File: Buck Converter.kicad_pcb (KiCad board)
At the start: 2 copper layers, 50 x 30 mm, 29 parts, among them J1 Conn_01x02, J2 Conn_01x02, SW1 SW_SPST, U1 LT3684xMSE

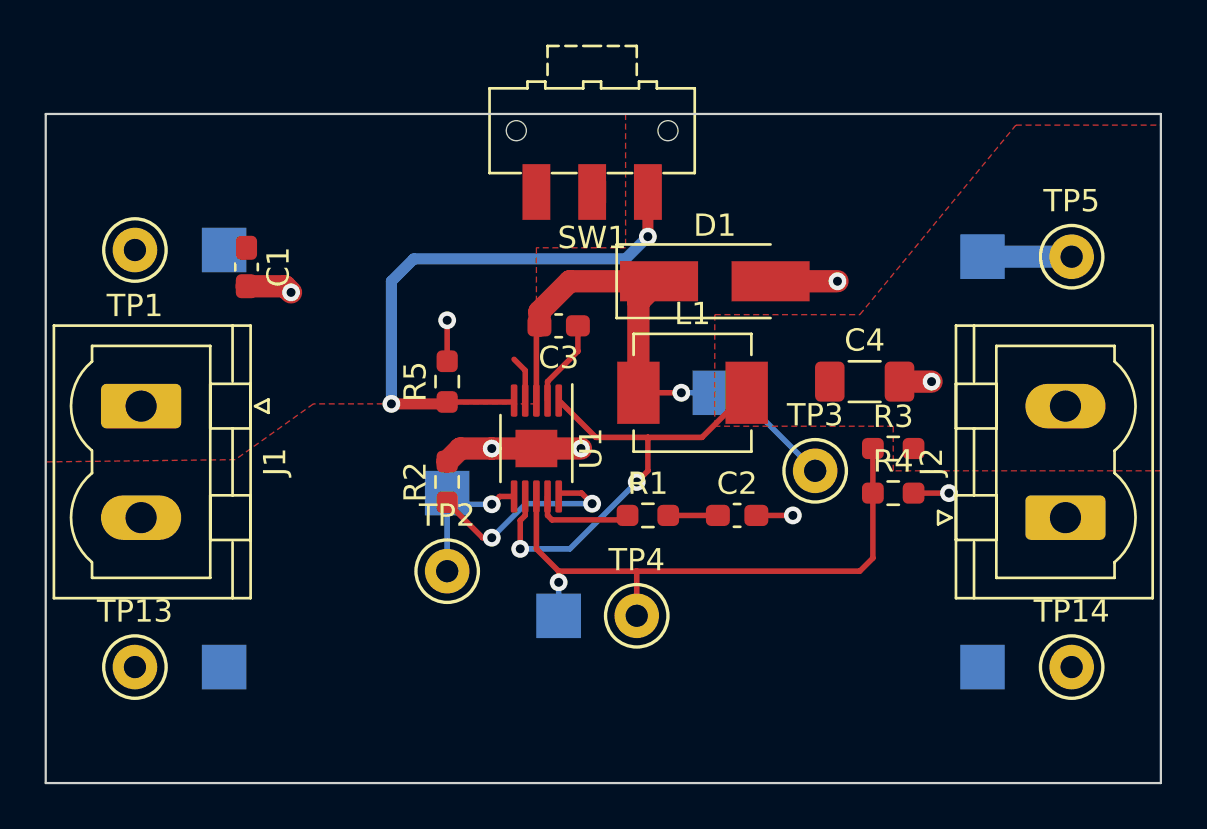
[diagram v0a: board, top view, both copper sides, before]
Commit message: Minor Tweaks
Updated PCB with the following recommendations:

1. Clean up the ERC and DRC issues.  The schematic has the USB connector without it being on the PCB; there's an unmade connection on TP6, and the silkscreen needs to be cleaned up.
2. Move the switch inward from the edge of the board.  The holes are close enough to the edge to cause some grief.
3. Move R5 a bit south.  It's an easy fix to clear up the path for VCC to get from J1.1 to U1.4.  Also to make way for:
3. Move C1 closer to the IC.  The bypass caps should be as close as possible to their associated ICs.
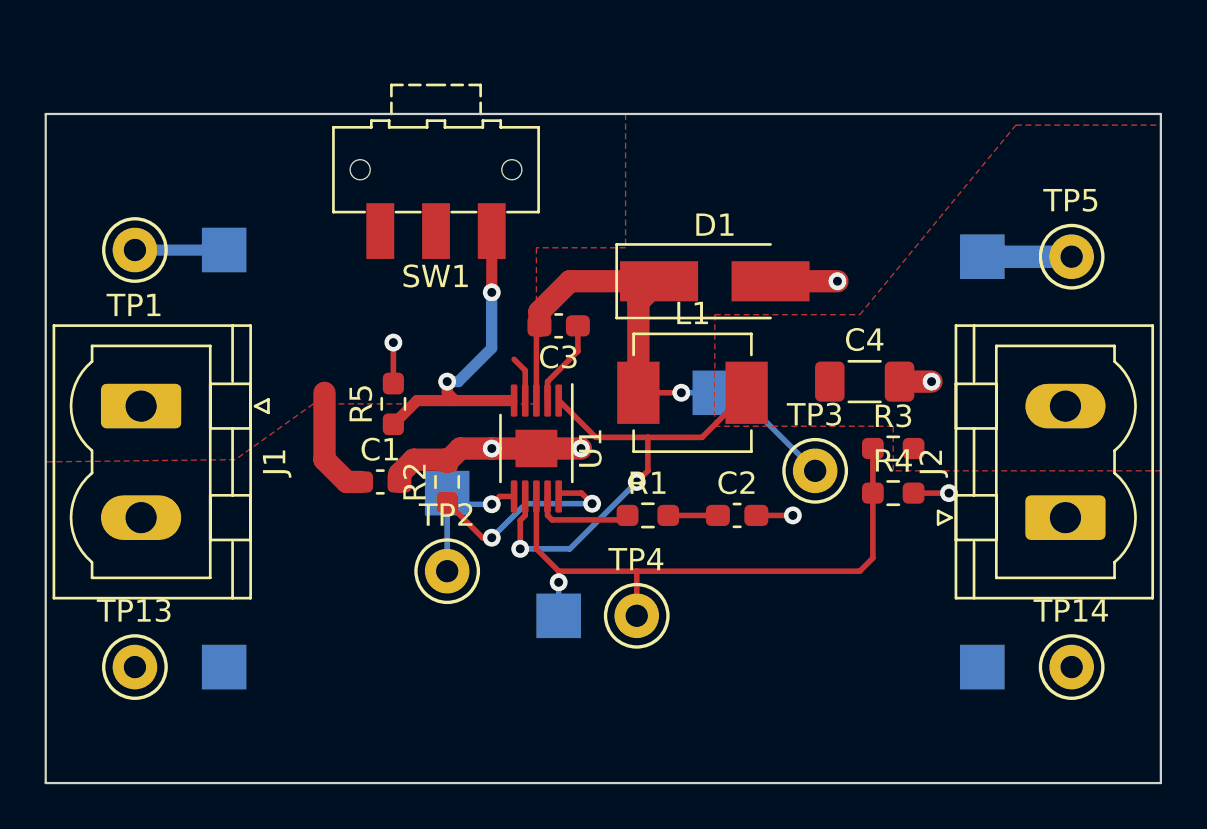
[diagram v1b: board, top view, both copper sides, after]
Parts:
- moved C1 11.4 mm to (115.0, 115.5), turned to 0 degrees
- moved SW1 7.22 mm to (117.5, 101.5)
- moved R5 2.61 mm to (115.6, 112.0)
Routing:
- net Net-(R5-Pad1): track 25.4 -> 15.1 mm
- net VCC: track 3.68 -> 11.3 mm
- net GND: track 17.9 -> 18.5 mm, vias 8 -> 7
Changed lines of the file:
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@@
   )
   (footprint "Resistor_SMD:R_0603_1608Metric_Pad0.98x0.95mm_HandSolder" (layer "F.Cu")
-    (at 118 111 90)
+    (at 115.5875 112 90)
     (descr "Resistor SMD 0603 (1608 Metric), square (rectangular) end terminal, IPC_7351 nominal with elongated pad for handsoldering. (Body size source: IPC-SM-782 page 72, https://www.pcb-3d.com/wordpress/wp-content/uploads/ipc-sm-782a_amendment_1_and_2.pdf), generated with kicad-footprint-generator")
     (tags "resistor handsolder")
@@
   )
   (footprint "Capacitor_SMD:C_0603_1608Metric_Pad1.08x0.95mm_HandSolder" (layer "F.Cu")
-    (at 109 105.8625 -90)
+    (at 115 115.5)
     (descr "Capacitor SMD 0603 (1608 Metric), square (rectangular) end terminal, IPC_7351 nominal with elongated pad for handsoldering. (Body size source: IPC-SM-782 page 76, https://www.pcb-3d.com/wordpress/wp-content/uploads/ipc-sm-782a_amendment_1_and_2.pdf), generated with kicad-footprint-generator")
     (tags "capacitor handsolder")
@@
     (property "Sheetname" "")
     (attr smd)
-    (fp_text reference "C1" (at 0 -1.43 90) (layer "F.SilkS")
-      (effects (font (size 1 1) (thickness 0.15)))
-    )
-    (fp_text value "2.2uF" (at 0 1.43 90) (layer "F.Fab")
-      (effects (font (size 1 1) (thickness 0.15)))
-    )
-    (fp_text user "${REFERENCE}" (at 0 0 90) (layer "F.Fab")
+    (fp_text reference "C1" (at 0 -1.43) (layer "F.SilkS")
+      (effects (font (size 1 1) (thickness 0.15)))
+    )
+    (fp_text value "2.2uF" (at 0 1.43) (layer "F.Fab")
+      (effects (font (size 1 1) (thickness 0.15)))
+    )
+    (fp_text user "${REFERENCE}" (at 0 0) (layer "F.Fab")
       (effects (font (size 0.4 0.4) (thickness 0.06)))
     )
@@
     (fp_line (start 0.8 0.4) (end -0.8 0.4) (layer "F.Fab") (width 0.1))
     (fp_line (start -0.8 -0.4) (end 0.8 -0.4) (layer "F.Fab") (width 0.1))
-    (pad "1" smd roundrect (at -0.8625 0 270) (size 1.075 0.95) (layers "F.Cu" "F.Paste" "F.Mask") (roundrect_rratio 0.25)
+    (pad "1" smd roundrect (at -0.8625 0) (size 1.075 0.95) (layers "F.Cu" "F.Paste" "F.Mask") (roundrect_rratio 0.25)
       (net 1 "VCC") (pintype "passive"))
-    (pad "2" smd roundrect (at 0.8625 0 270) (size 1.075 0.95) (layers "F.Cu" "F.Paste" "F.Mask") (roundrect_rratio 0.25)
+    (pad "2" smd roundrect (at 0.8625 0) (size 1.075 0.95) (layers "F.Cu" "F.Paste" "F.Mask") (roundrect_rratio 0.25)
       (net 2 "GND") (pintype "passive"))
     (model "${KICAD6_3DMODEL_DIR}/Capacitor_SMD.3dshapes/C_0603_1608Metric.wrl"
@@
   )
   (footprint "Button_Switch_SMD:SW_SPDT_CK-JS102011SAQN" (layer "F.Cu")
-    (at 124.5 99.75 180)
+    (at 117.5 101.5 180)
     (descr "Sub-miniature slide switch, right-angle, http://www.ckswitches.com/media/1422/js.pdf")
     (tags "switch spdt")
@@
   )
   (gr_rect (start 100 99) (end 150 129) (layer "Edge.Cuts") (width 0.1) (fill none))
-  (segment (start 124.5 103.125) (end 124.5 102.5) (width 1) (layer "F.Cu") (net 1))
+  (segment (start 114.1375 115.5) (end 113.5 115.5) (width 1) (layer "F.Cu") (net 1))
+  (segment (start 112.5 114.5) (end 112.5 111.5) (width 1) (layer "F.Cu") (net 1))
   (segment (start 121.5 111.85) (end 121.5 110.5) (width 0.25) (layer "F.Cu") (net 1))
+  (segment (start 113.5 115.5) (end 112.5 114.5) (width 1) (layer "F.Cu") (net 1))
   (segment (start 121.5 110.5) (end 121 110) (width 0.25) (layer "F.Cu") (net 1))
-  (segment (start 125 103) (end 125 102) (width 0.25) (layer "F.Cu") (net 1))
-  (segment (start 110.725 106.725) (end 111 107) (width 1) (layer "F.Cu") (net 2))
-  (segment (start 109 106.725) (end 110.725 106.725) (width 1) (layer "F.Cu") (net 2))
-  (segment (start 118 110.0875) (end 118 108.25) (width 0.25) (layer "F.Cu") (net 2))
+  (segment (start 108.1 105) (end 108 105.1) (width 0.25) (layer "B.Cu") (net 1))
+  (segment (start 104 105.1) (end 108 105.1) (width 0.5) (layer "B.Cu") (net 1))
+  (segment (start 115.5875 111.0875) (end 115.5875 109.25) (width 0.25) (layer "F.Cu") (net 2))
   (segment (start 138.28125 111) (end 139.71875 111) (width 1) (layer "F.Cu") (net 2))
+  (segment (start 115.8625 115.5) (end 115.8625 115.1375) (width 1) (layer "F.Cu") (net 2))
   (segment (start 122 114) (end 120 114) (width 1) (layer "F.Cu") (net 2))
   (segment (start 131.8625 117) (end 133.5 117) (width 0.25) (layer "F.Cu") (net 2))
   (segment (start 138.9125 116) (end 140.5 116) (width 0.25) (layer "F.Cu") (net 2))
+  (segment (start 117.9125 114.5) (end 118 114.5875) (width 1) (layer "F.Cu") (net 2))
+  (segment (start 116.5 114.5) (end 117.9125 114.5) (width 1) (layer "F.Cu") (net 2))
   (segment (start 122 114) (end 124 114) (width 1) (layer "F.Cu") (net 2))
   (segment (start 132.5 106.5) (end 135.5 106.5) (width 1) (layer "F.Cu") (net 2))
   (segment (start 120 114) (end 118.5875 114) (width 1) (layer "F.Cu") (net 2))
   (segment (start 118.5875 114) (end 118 114.5875) (width 1) (layer "F.Cu") (net 2))
+  (segment (start 115.8625 115.1375) (end 116.5 114.5) (width 1) (layer "F.Cu") (net 2))
   (via (at 140.5 116) (size 0.8) (drill 0.4) (layers "F.Cu" "B.Cu") (net 2))
   (via (at 135.5 106.5) (size 0.8) (drill 0.4) (layers "F.Cu" "B.Cu") (net 2))
   (via (at 120 114) (size 0.8) (drill 0.4) (layers "F.Cu" "B.Cu") (net 2))
-  (via (at 118 108.25) (size 0.8) (drill 0.4) (layers "F.Cu" "B.Cu") (net 2))
+  (via (at 115.5875 109.25) (size 0.8) (drill 0.4) (layers "F.Cu" "B.Cu") (net 2))
   (via (at 133.5 117) (size 0.8) (drill 0.4) (layers "F.Cu" "B.Cu") (net 2))
-  (via (at 111 107) (size 0.8) (drill 0.4) (layers "F.Cu" "B.Cu") (net 2))
   (via (at 139.71875 111) (size 0.8) (drill 0.4) (layers "F.Cu" "B.Cu") (net 2))
   (via (at 124 114) (size 0.8) (drill 0.4) (layers "F.Cu" "B.Cu") (net 2))
@@
   (segment (start 126.5735 107.4265) (end 127.5 106.5) (width 1) (layer "F.Cu") (net 4))
   (segment (start 127.5 106.5) (end 123.5 106.5) (width 1) (layer "F.Cu") (net 4))
+  (segment (start 122 108.6375) (end 122.1375 108.5) (width 0.25) (layer "F.Cu") (net 4))
   (segment (start 128.5 111.5) (end 126.5735 111.5) (width 0.25) (layer "F.Cu") (net 4))
   (segment (start 123.5 106.5) (end 122.1375 107.8625) (width 1) (layer "F.Cu") (net 4))
   (segment (start 122.1375 107.8625) (end 122.1375 108.5) (width 1) (layer "F.Cu") (net 4))
+  (segment (start 126.5735 111.5) (end 126.5735 107.4265) (width 1) (layer "F.Cu") (net 4))
   (segment (start 122 111.85) (end 122 108.6375) (width 0.25) (layer "F.Cu") (net 4))
-  (segment (start 126.5735 111.5) (end 126.5735 107.4265) (width 1) (layer "F.Cu") (net 4))
-  (segment (start 122 108.6375) (end 122.1375 108.5) (width 0.25) (layer "F.Cu") (net 4))
   (via (at 128.5 111.5) (size 0.8) (drill 0.4) (layers "F.Cu" "B.Cu") (net 4))
   (segment (start 130 111.5) (end 128.5 111.5) (width 0.25) (layer "B.Cu") (net 4))
@@
   (via (at 123 120) (size 0.8) (drill 0.4) (layers "F.Cu" "B.Cu") (net 9))
   (segment (start 123 120) (end 123 121.5) (width 0.25) (layer "B.Cu") (net 9))
-  (segment (start 127 102.5) (end 127 104.5) (width 0.5) (layer "F.Cu") (net 10))
-  (segment (start 118 111.9125) (end 120.9375 111.9125) (width 0.25) (layer "F.Cu") (net 10))
-  (segment (start 115.5 112) (end 117.9125 112) (width 0.5) (layer "F.Cu") (net 10))
-  (segment (start 117.9125 112) (end 118 111.9125) (width 0.5) (layer "F.Cu") (net 10))
-  (segment (start 120.9375 111.9125) (end 121 111.85) (width 0.25) (layer "F.Cu") (net 10))
-  (via (at 127 104.5) (size 0.8) (drill 0.4) (layers "F.Cu" "B.Cu") (net 10))
-  (via (at 115.5 112) (size 0.8) (drill 0.4) (layers "F.Cu" "B.Cu") (net 10))
-  (segment (start 127 104.5) (end 126 105.5) (width 0.5) (layer "B.Cu") (net 10))
-  (segment (start 115.5 106.5) (end 115.5 112) (width 0.5) (layer "B.Cu") (net 10))
-  (segment (start 126 105.5) (end 116.5 105.5) (width 0.5) (layer "B.Cu") (net 10))
-  (segment (start 116.5 105.5) (end 115.5 106.5) (width 0.5) (layer "B.Cu") (net 10))
+  (segment (start 118.35 111.85) (end 120.90048 111.85) (width 0.5) (layer "F.Cu") (net 10))
+  (segment (start 118 111.5) (end 118 111) (width 0.5) (layer "F.Cu") (net 10))
+  (segment (start 116.65 111.85) (end 118.35 111.85) (width 0.5) (layer "F.Cu") (net 10))
+  (segment (start 120 107) (end 120 103.75) (width 0.5) (layer "F.Cu") (net 10))
+  (segment (start 118.35 111.85) (end 118 111.5) (width 0.5) (layer "F.Cu") (net 10))
+  (segment (start 115.5875 112.9125) (end 116.65 111.85) (width 0.5) (layer "F.Cu") (net 10))
+  (via (at 120 107) (size 0.8) (drill 0.4) (layers "F.Cu" "B.Cu") (net 10))
+  (via (at 118 111) (size 0.8) (drill 0.4) (layers "F.Cu" "B.Cu") (net 10))
+  (segment (start 118 111) (end 118.5 111) (width 0.5) (layer "B.Cu") (net 10))
+  (segment (start 118.5 111) (end 120 109.5) (width 0.5) (layer "B.Cu") (net 10))
+  (segment (start 120 109.5) (end 120 107) (width 0.5) (layer "B.Cu") (net 10))
   (segment (start 120.35 116.15) (end 120 116.5) (width 0.25) (layer "F.Cu") (net 11))
   (segment (start 121 116.15) (end 120.35 116.15) (width 0.25) (layer "F.Cu") (net 11))

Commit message: Made layout changes as per Seth's reccomendations
1. Clean up the ERC and DRC issues.  The schematic has the USB connector without it being on the PCB; there's an unmade connection on TP6, and the silkscreen needs to be cleaned up.
2. Move the switch inward from the edge of the board.  The holes are close enough to the edge to cause some grief.
3. Move R5 a bit south.  It's an easy fix to clear up the path for VCC to get from J1.1 to U1.4.  Also to make way for:
3. Move C1 closer to the IC.  The bypass caps should be as close as possible to their associated ICs.

4. The connection between U1.3 and C3.2 is a bit thin.  That's part of the power path, however, I also recognize that it's a pretty tight fit already, so there's only so much you can do.  Try to widen that up as much as you can.

5. Adjusted silkscreen to fix warnings
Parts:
- moved C1 6.02 mm to (119.5, 111.5), turned to -90 degrees
- moved R5 2.00 mm to (115.5, 114.0), turned to -90 degrees
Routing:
- net VCC: track 11.3 -> 6.06 mm
- net GND: track 18.5 -> 18.4 mm, vias 7 -> 6
- net Net-(R5-Pad1): track 15.1 -> 15.2 mm, vias 2 -> 3

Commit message: 5V, VCC, GND and Version silkscreen
Added front silkscreen text in top left corner of board for version number. Labeled 5V, VCC, and GND terminals in back silkscreen text.
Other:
- board text added: "+5V"
- board text added: "GND"
- board text added: "V1"
- board text added: "VCC"
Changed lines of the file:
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@@
     (property "Sheetname" "")
     (attr through_hole)
-    (fp_text reference "TP1" (at 0 2.6) (layer "F.SilkS")
+    (fp_text reference "TP1" (at -3.25 0.1) (layer "F.SilkS")
       (effects (font (size 1 1) (thickness 0.15)))
     )
@@
   )
   (gr_rect (start 100 99) (end 150 129) (layer "Edge.Cuts") (width 0.1) (fill none))
+  (gr_text "GND\n" (at 141.25 117) (layer "B.SilkS")
+    (effects (font (size 1 1) (thickness 0.15)) (justify mirror))
+  )
+  (gr_text "VCC" (at 108.75 112) (layer "B.SilkS")
+    (effects (font (size 1 1) (thickness 0.15)) (justify mirror))
+  )
+  (gr_text "+5V" (at 141.5 112.25) (layer "B.SilkS")
+    (effects (font (size 1 1) (thickness 0.15)) (justify mirror))
+  )
+  (gr_text "GND\n" (at 108.75 117.25) (layer "B.SilkS")
+    (effects (font (size 1 1) (thickness 0.15)) (justify mirror))
+  )
+  (gr_text "V1\n" (at 102.5 101.25) (layer "F.SilkS")
+    (effects (font (size 1.5 1.5) (thickness 0.3)))
+  )
   (segment (start 121.5 111.85) (end 121.5 110.5) (width 0.25) (layer "F.Cu") (net 1))
   (segment (start 121.5 110.5) (end 121 110) (width 0.25) (layer "F.Cu") (net 1))
